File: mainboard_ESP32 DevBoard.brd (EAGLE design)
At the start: 56.3 x 89.8 mm, 37 parts, among them IC1 LM358N, IC2 LM833N, IC3 74HC08N, K1 AQH213, X1 JST-XH-02-PIN-LONG-PAD, X2 JST-XH-04-PIN-LONG-PAD, X3 1751248, X4 1751248

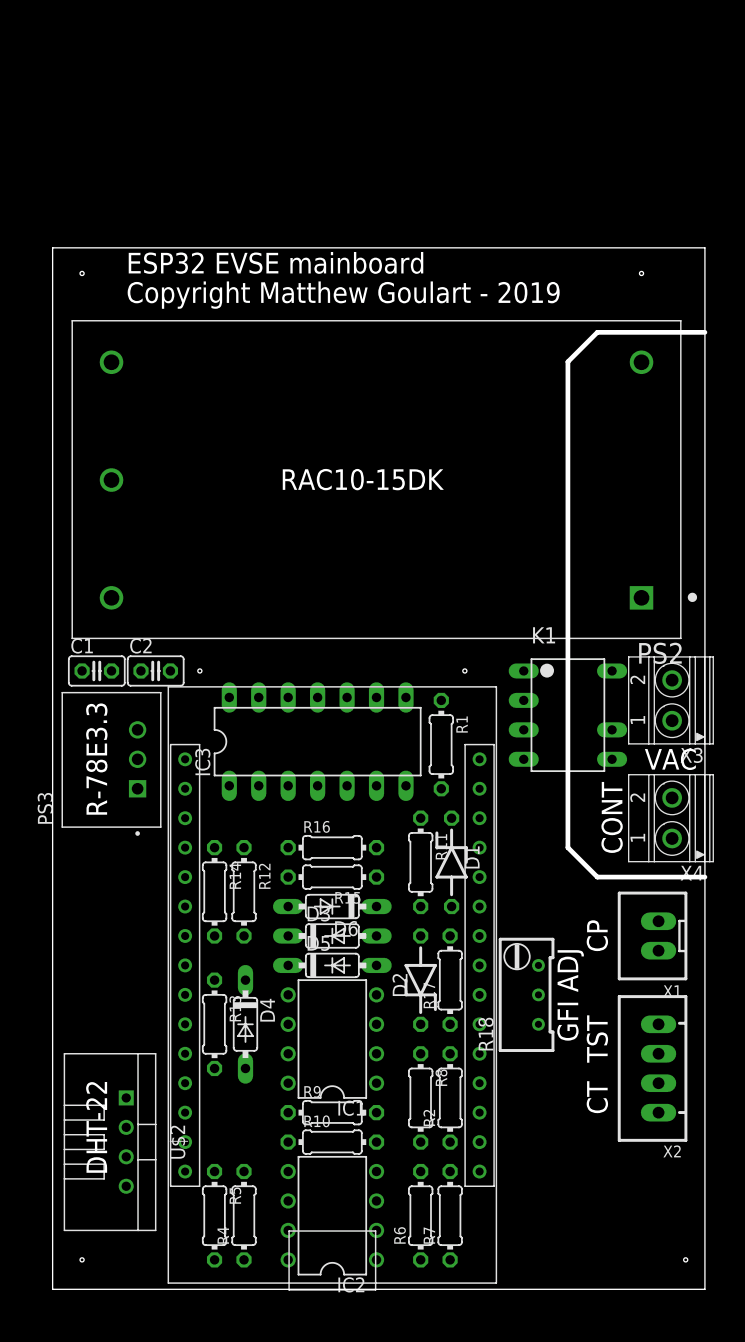
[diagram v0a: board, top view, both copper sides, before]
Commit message: Completed routing first try of board. Some pin changes to fit the board better. Added puldown and jumper to prevent accidental coil energize.
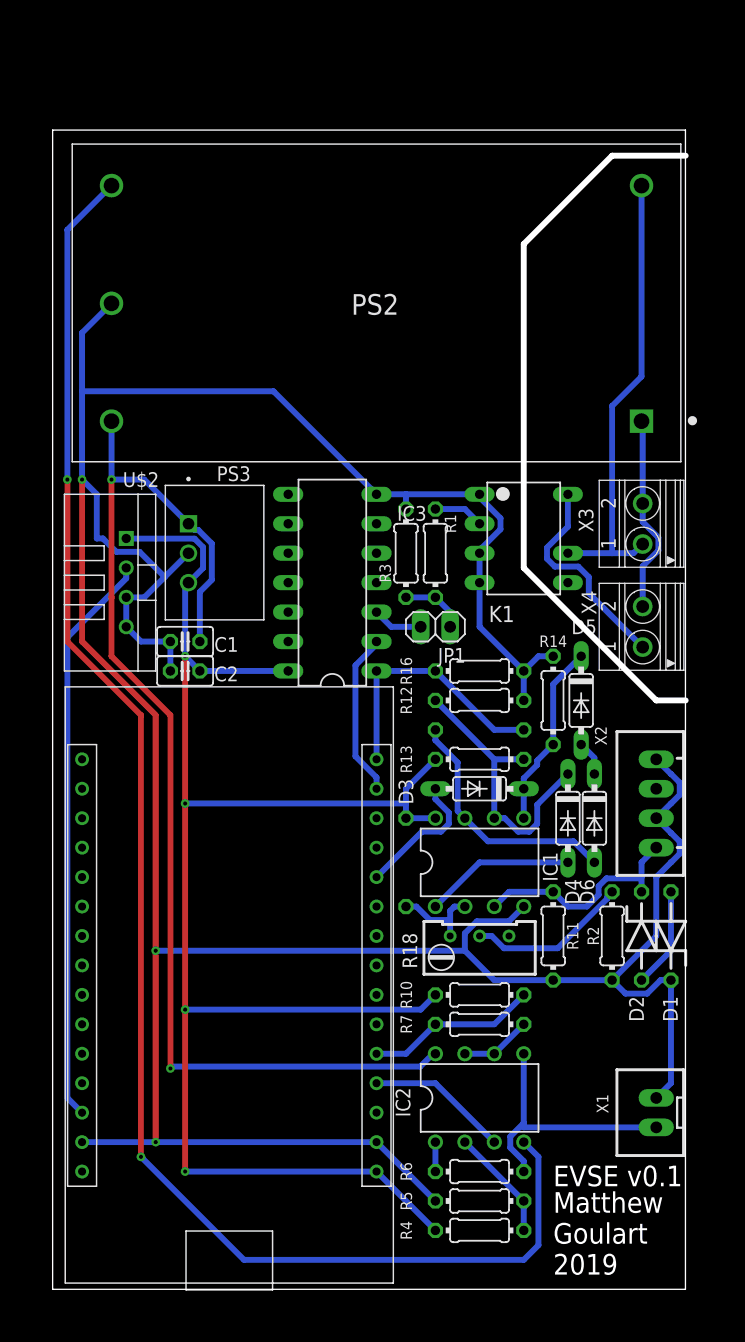
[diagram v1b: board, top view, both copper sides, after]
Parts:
- removed R8: 220K, rcl:0204/7
- removed R9: 100K, rcl:0204/7
- added JP1: (no value), pinhead:1X02
- added R3: 330, rcl:0204/7
- D1, D2: value (none) -> 3.3V
- moved U$2 48.3 mm to (6.35, 61.0)
- moved R14 33.6 mm to (43.2, 50.8)
- moved D4 33.0 mm to (44.5, 40.6)
- moved R13 32.3 mm to (36.8, 45.7), turned to 180 degrees
- moved D5 31.4 mm to (45.6, 50.8), turned to 270 degrees
- moved R12 26.2 mm to (36.8, 50.8), turned to 180 degrees
- moved D6 23.9 mm to (46.7, 40.6), turned to 270 degrees
- moved R5 22.9 mm to (36.8, 7.62), turned to 0 degrees
- moved X2 22.9 mm to (52.1, 41.9)
- moved R4 20.4 mm to (36.8, 5.08), turned to 180 degrees
- moved D1 20.0 mm to (53.3, 30.5), turned to 90 degrees
- moved PS3 19.9 mm to (14.0, 63.5), turned to 270 degrees
- moved IC1 19.8 mm to (36.8, 36.8), turned to 0 degrees
- moved R16 19.8 mm to (36.8, 53.3), turned to 180 degrees
- moved R2 19.8 mm to (48.3, 30.5)
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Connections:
- removed net N$18: R10.2, R7.2, R8.2
- new net N$3: JP1.1, R1.2, R3.1
- net +15V: no longer IC1.8, R13.2, R17.1
- net +3V3: now also IC1.8, R13.2, R17.1
- net CP_PWM: now also U$3.GPIO2; no longer U$3.GPIO4
- net CP_READ: now also R10.2, R7.2, U$3.GPIO4; no longer R8.1, R9.2, U$3.GPIO2
- net ENER: now also JP1.2; no longer R1.2
- net GFI_INT: now also U$3.GPIO23
- net GND: now also R3.2; no longer R9.1
- net MCU_ENER: now also U$3.GPIO22; no longer U$3.GPIO32
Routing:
- net GND: track 0.00 -> 289.7 mm, vias 0 -> 3
- net +3V3: track 0.00 -> 144.4 mm, vias 0 -> 4
- net -15V: track 0.00 -> 135.9 mm, vias 0 -> 2
- net +15V: track 0.00 -> 101.1 mm, vias 0 -> 2
- net DHT_DATA: track 0.00 -> 49.6 mm
- net VPP: track 0.00 -> 39.5 mm
- net N$14: track 0.00 -> 24.7 mm
- net CP: track 0.00 -> 22.9 mm
- net GFI_INT: track 0.00 -> 22.4 mm
- net N$11: track 0.00 -> 21.4 mm
- net CT: track 0.00 -> 19.6 mm
- net ENER_COIL: track 0.00 -> 18.5 mm
- net AGND: track 0.00 -> 17.2 mm
- net N$13: track 0.00 -> 16.0 mm
- net CP_READ: track 0.00 -> 14.8 mm
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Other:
- board size 56.3 x 89.8 mm -> 54.6 x 100 mm
- board text added: "EVSE v0.1"
- board text added: "Matthew Goulart 2019"
- board text removed: "CONT"
- board text removed: "CP"
- board text removed: "CT"
- board text removed: "Copyright Matthew Goulart - 2019"
- board text removed: "DHT-22"
- board text removed: "ESP32 EVSE mainboard"
- board text removed: "GFI ADJ"
- board text removed: "R-78E3.3"
- board text removed: "RAC10-15DK"
- board text removed: "TST"
- board text removed: "VAC"

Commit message: Tweaked resistor on GFI circuit to allow 3.3v logic to set the latch
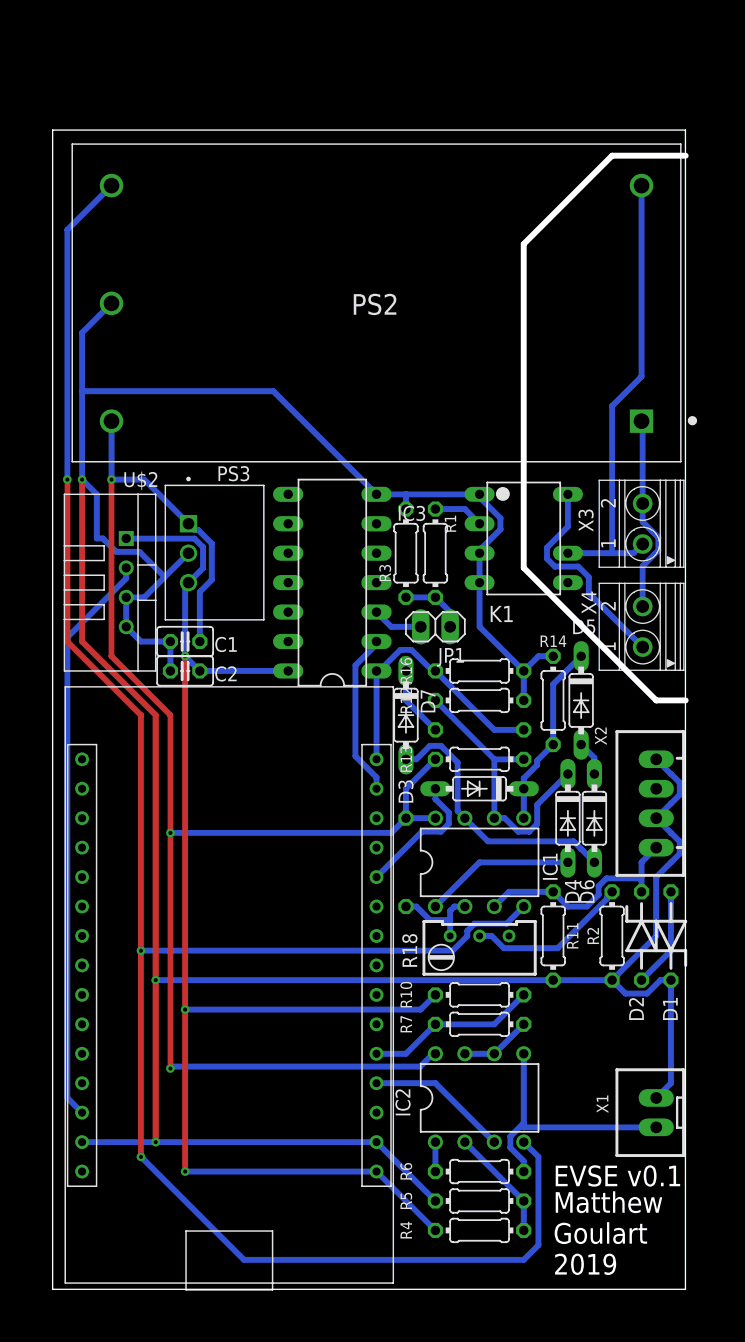
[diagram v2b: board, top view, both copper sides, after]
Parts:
- added D7: 1N4148DO35-7, diode:DO35-7
- D1, D2: value 3.3V -> 12V
- R12: value 10K -> 1.5K
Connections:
- removed net N$11: D6.A, IC1.7, R15.2
- new net N$4: D6.A, D7.A, IC1.7
- new net N$7: D7.C, R15.2
- net +15V: now also IC1.8, R13.2, R17.1
- net +3V3: no longer IC1.8, R13.2, R17.1
- net -15V: now also IC1.4
- net GND: no longer IC1.4
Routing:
- net -15V: track 135.9 -> 170.8 mm, vias 2 -> 3
- net +15V: track 101.1 -> 130.7 mm, vias 2 -> 3
- net +3V3: track 144.4 -> 116.7 mm, vias 4 -> 3
- net N$4: track 0.00 -> 23.4 mm
- net N$11: track 21.4 -> 0.00 mm
- net GND: track 289.7 -> 281.1 mm
- net N$7: track 0.00 -> 6.13 mm
- net GFI_INT: track 22.4 -> 23.9 mm

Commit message: Added header to disconnect 3.3v output from esp to 3.3 rail. Added LED to indicate when contactor is energized. Added I2C connector. Added mounting holes.
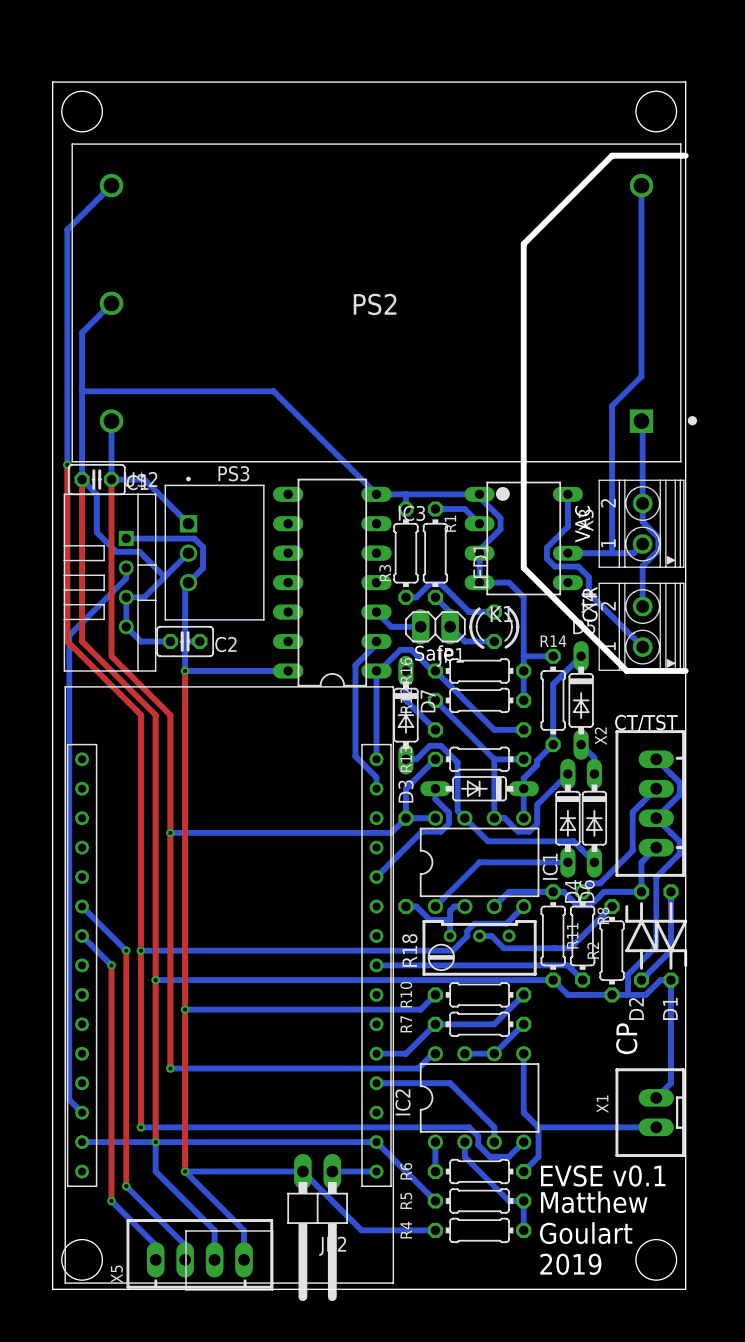
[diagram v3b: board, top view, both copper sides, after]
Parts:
- added JP2: (no value), pinhead:1X02/90
- added LED1: (no value), led:LED3MM
- added R8: 750, rcl:0204/7
- added X5: JST-XH-04-PIN-LONG-PAD, Rembrandt Electronics - JST XH Connectors v1-0:JST-XH-04-PACKAGE-LONG-PAD
- R3: value 330 -> 130
- moved C1 15.9 mm to (3.81, 69.8)
- moved C2 2.54 mm to (11.4, 55.9)
- moved R2 1.27 mm to (48.3, 29.2)
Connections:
- new net GFI_TST_SIG: R8.2, U$3.GPIO5
- new net N$10: JP2.1, U$3.3.3V
- new net N$8: LED1.K, R3.1
- new net SCL: U$3.GPIO33, X5.1
- new net SDA: U$3.GPIO32, X5.2
- net +3V3: now also JP2.2, X5.4; no longer U$3.3.3V
- net GFI_TEST: now also R8.1
- net GND: now also X5.3
- net N$3: now also LED1.A; no longer R3.1
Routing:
- net SDA: track 0.00 -> 34.2 mm, vias 0 -> 2
- net SCL: track 0.00 -> 30.6 mm, vias 0 -> 2
- net GFI_TST_SIG: track 0.00 -> 18.3 mm
- net -15V: track 170.8 -> 155.3 mm
- net GFI_TEST: track 0.00 -> 12.0 mm
- net +15V: track 130.7 -> 119.1 mm, vias 3 -> 2
- net GND: track 281.1 -> 292.3 mm, vias 3 -> 2
- net +3V3: track 116.7 -> 127.1 mm
- net N$8: track 0.00 -> 9.11 mm
- net N$10: track 0.00 -> 3.81 mm
- net N$3: track 5.61 -> 7.40 mm
- net CP: track 22.9 -> 21.4 mm
- net CT: track 19.6 -> 18.5 mm
- net N$15: track 9.72 -> 10.5 mm
- net CP_PWM: track 12.3 -> 13.0 mm
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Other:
- board size 54.6 x 100 mm -> 54.6 x 104.1 mm
- board text added: "CP"
- board text added: "CT/TST"
- board text added: "CTR"
- board text added: "Safe"
- board text added: "VAC"

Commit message: Made all traces as big as possible. Pads also. Added some layers for CAM outputs. Added cam job file
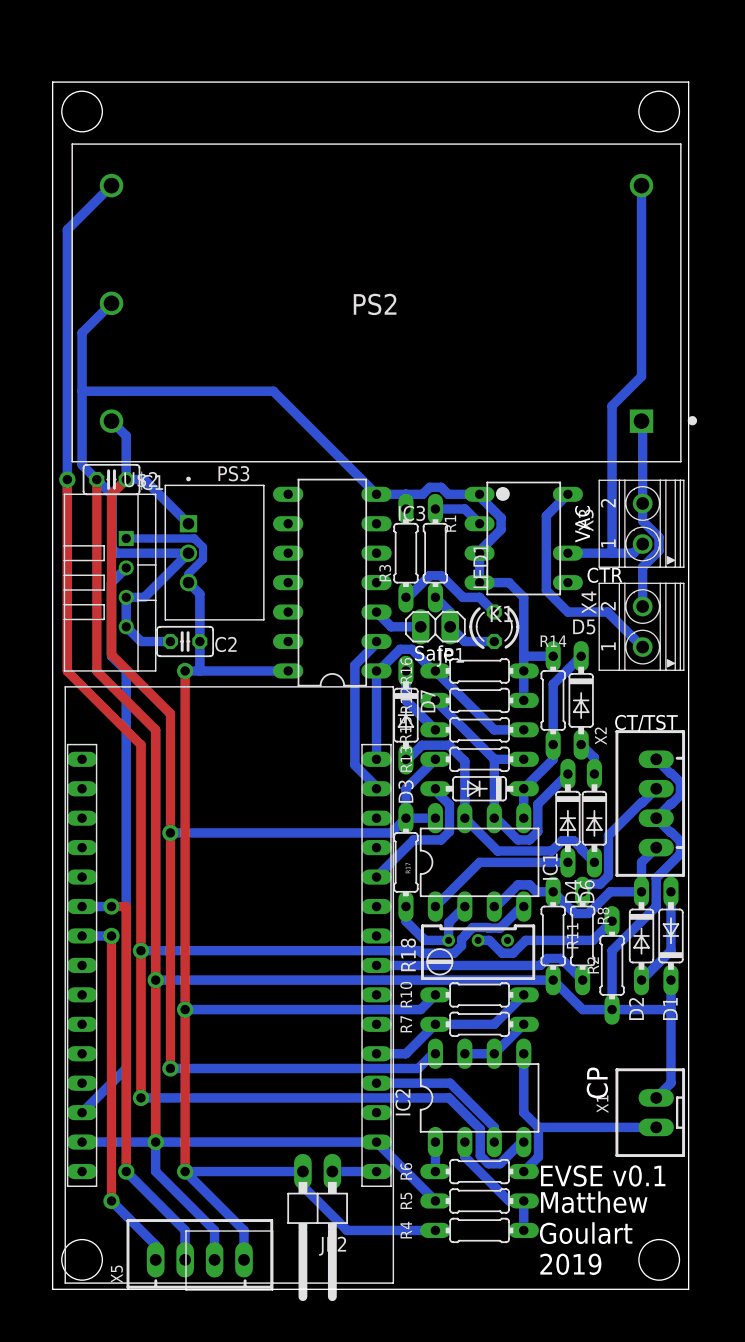
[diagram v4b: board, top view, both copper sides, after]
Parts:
- D1, D2: device diode:ZDIO-7.5 -> Passive:DO35-7
- IC1: value LM358N -> OP-AMP-2-LONG; device linear:DIL08 -> Op Amp:DIL08-LONG
- IC2: value LM833N -> OP-AMP-2-LONG; device linear:DIL08 -> Op Amp:DIL08-LONG
- R1, R10, R11, R12, R13, R14, R15, R16, R17, R2, R3, R4, R5, R6, R7, R8: device rcl:0204/7 -> Passive:0204/7-L
- moved C1 1.27 mm to (5.08, 69.8)
- moved R2 1.27 mm to (48.3, 27.9)
- moved R18 0.40 mm to (36.7, 28.8)
- flipped R15 to the top, turned to 180 degrees
- flipped R17 to the top
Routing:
- net GND: track 292.3 -> 295.6 mm
- net SDA: track 34.2 -> 36.4 mm
- net SCL: track 30.6 -> 32.1 mm
- net N$4: track 23.4 -> 24.6 mm
- net N$2: track 7.93 -> 9.14 mm
- net CT: track 18.5 -> 19.6 mm
- net N$14: track 24.7 -> 25.7 mm
- net ENER_COIL: track 18.5 -> 19.4 mm
- net N$8: track 9.11 -> 9.69 mm
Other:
- board size 54.6 x 104.1 mm -> 54.9 x 104.1 mm

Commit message: Updated ignore file. Made some adjustments after making the first board.
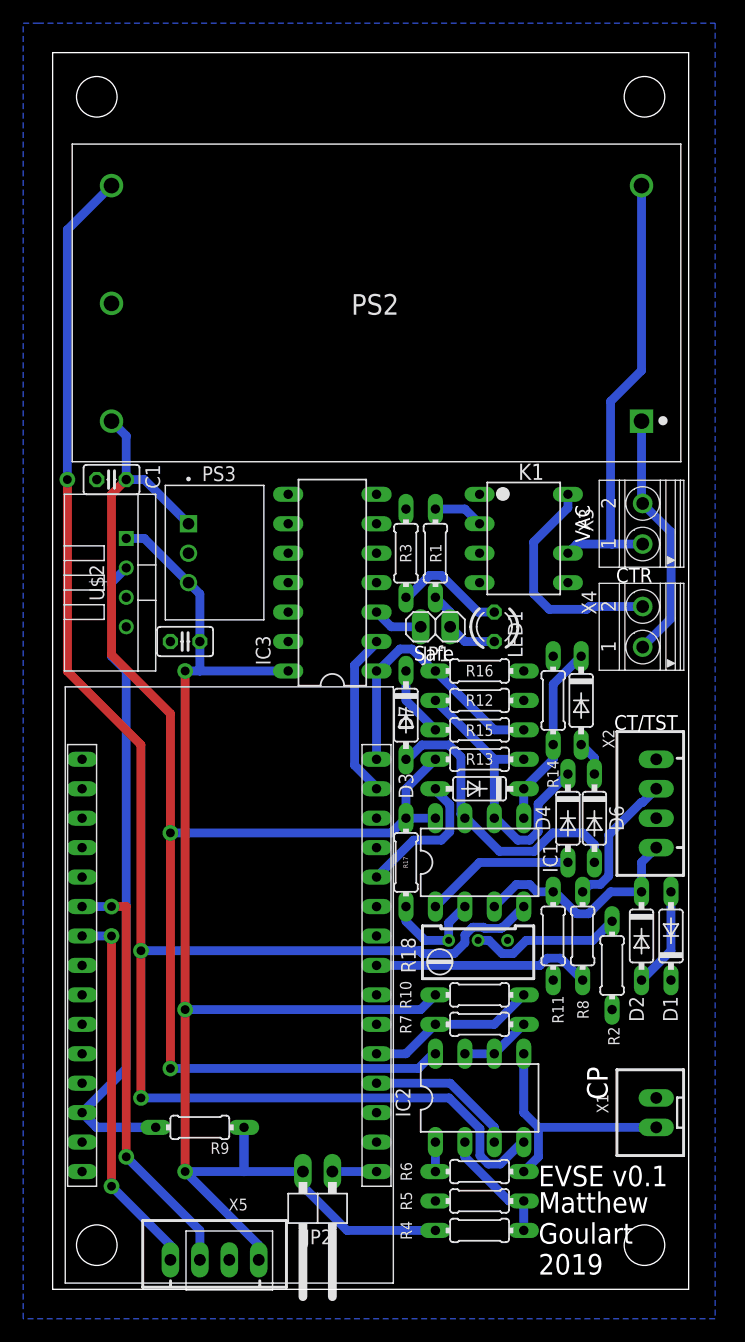
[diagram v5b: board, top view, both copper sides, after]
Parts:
- added R9: 240K, Passive:0204/7-L
- R11: value 412 -> 35.7K
- moved X5 1.27 mm to (14.0, 2.54)
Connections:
- net VPP renamed VACL
- removed net AGND: PS2.1, X3.2, X4.2
- new net VACN: PS2.1, X3.2, X4.1
- net +3V3: now also R9.1
- net DHT_DATA: now also R9.2
- net ENER_COIL: now also X4.2; no longer X4.1
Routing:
- net GND: track 295.6 -> 0.00 mm, vias 2 -> 0
- net VACN: track 0.00 -> 21.6 mm
- net AGND: track 17.2 -> 0.00 mm
- net DHT_DATA: track 49.6 -> 56.5 mm
- net N$4: track 24.6 -> 26.1 mm
- net +3V3: track 126.9 -> 127.7 mm
- net VACL: track 39.5 -> 38.9 mm
- net SDA: track 36.4 -> 36.9 mm
- net SCL: track 32.1 -> 32.6 mm
- added copper zone on layer 16, net GND
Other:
- board size 54.9 x 104.1 mm -> 54.9 x 106.7 mm

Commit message: Made board single-sided friendly (P2P wiring needed). Tweaked some more resistor values. Added missing resistor to CP read level shifter
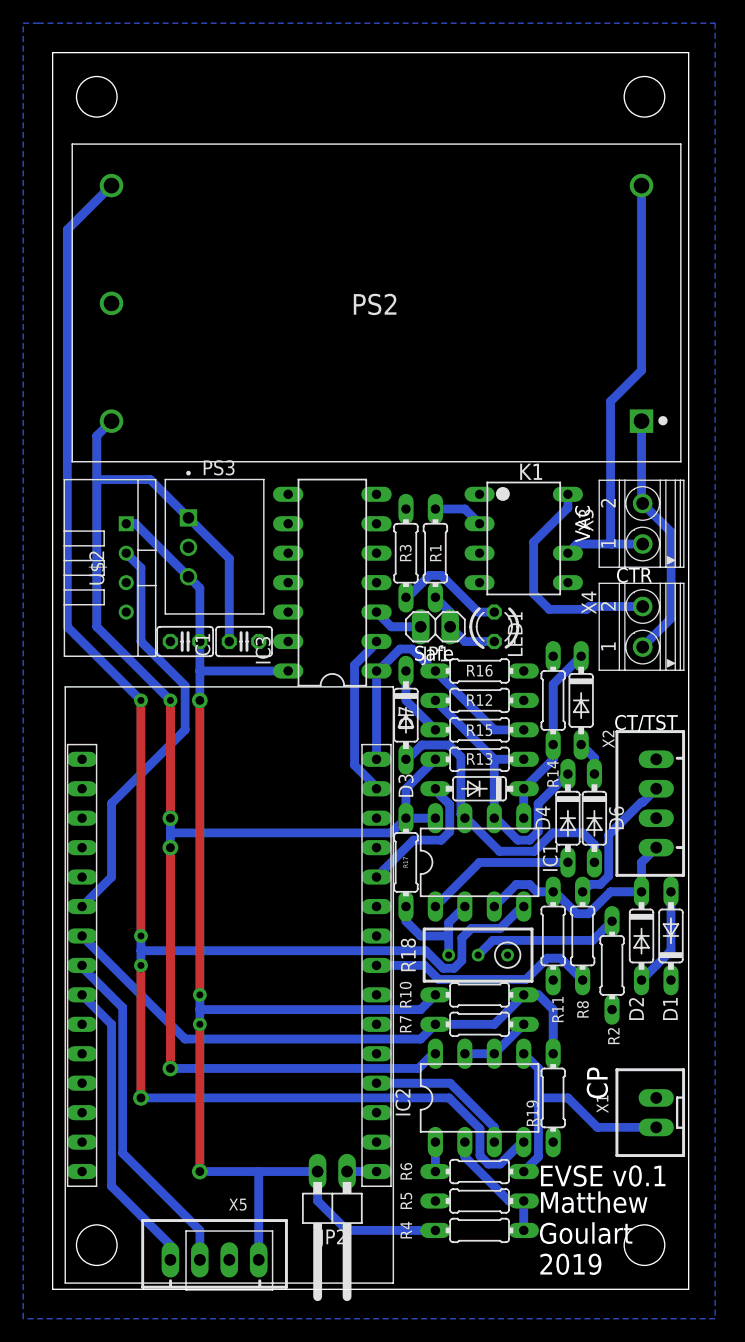
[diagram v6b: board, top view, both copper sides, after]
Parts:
- removed R9: 240K, Passive:0204/7-L
- added R19: 36K, Passive:0204/7-L
- R10: value 240K -> 24K
- R17: value 100K -> 10K
- R18: device rcl:RTRIM64W -> rcl:RTRIM3296W
- R2: value 13 -> 430
- R7: value 910K -> 91K
- moved C1 18.1 mm to (16.5, 55.9), turned to 0 degrees
- moved JP2 1.27 mm to (24.1, 6.35)
- moved U$2 1.27 mm to (6.35, 62.2)
- moved PS3 0.51 mm to (14.0, 64.0)
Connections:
- net +3V3: no longer R9.1
- net CP_READ: now also R19.2, U$3.GPIO33; no longer U$3.GPIO4
- net DHT_DATA: now also U$3.GPIO32; no longer R9.2, U$3.GPIO13
- net GND: now also R19.1
- net SCL: now also U$3.GPIO26; no longer U$3.GPIO33
- net SDA: now also U$3.GPIO25; no longer U$3.GPIO32
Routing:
- net CP_READ: track 14.8 -> 50.2 mm
- net DHT_DATA: track 56.5 -> 36.3 mm
- net +15V: track 118.8 -> 133.3 mm, vias 2 -> 4
- net +3V3: track 127.7 -> 119.0 mm, vias 3 -> 4
- net SDA: track 36.9 -> 29.6 mm, vias 2 -> 0
- net SCL: track 32.6 -> 26.0 mm, vias 2 -> 0
- net -15V: track 155.7 -> 157.4 mm, vias 3 -> 4
- net N$10: track 3.81 -> 2.54 mm
- net N$2: track 9.14 -> 10.2 mm
- net CP: track 21.4 -> 22.4 mm
- net GFI_TST_SIG: track 18.8 -> 19.8 mm
